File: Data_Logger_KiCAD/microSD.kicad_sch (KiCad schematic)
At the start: 9 parts, among them J3 Micro_SD_Card

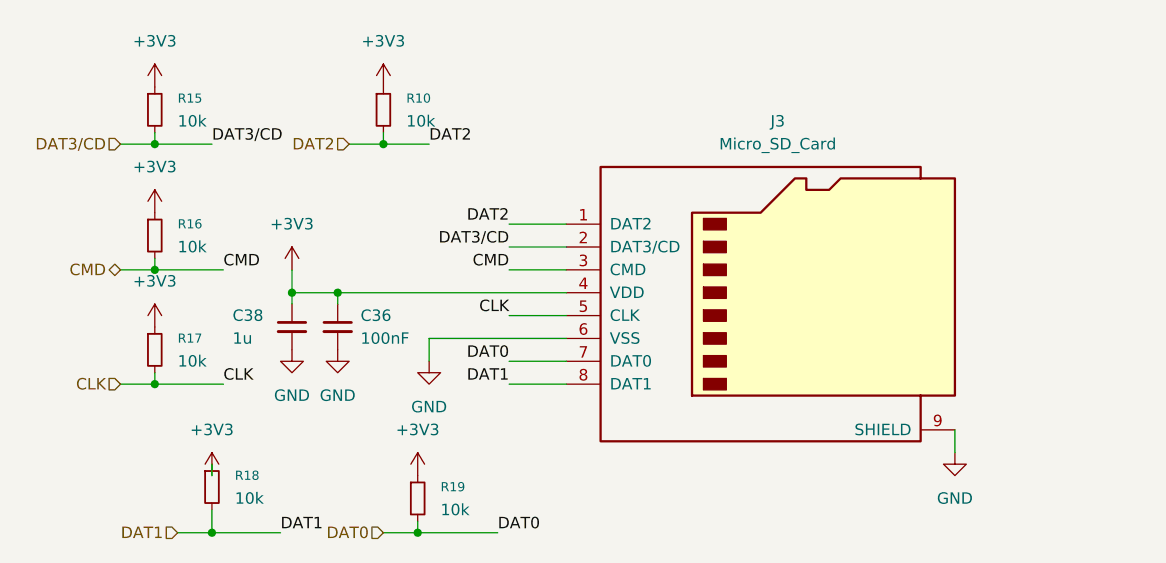
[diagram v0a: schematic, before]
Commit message: footprint + sd tweaks
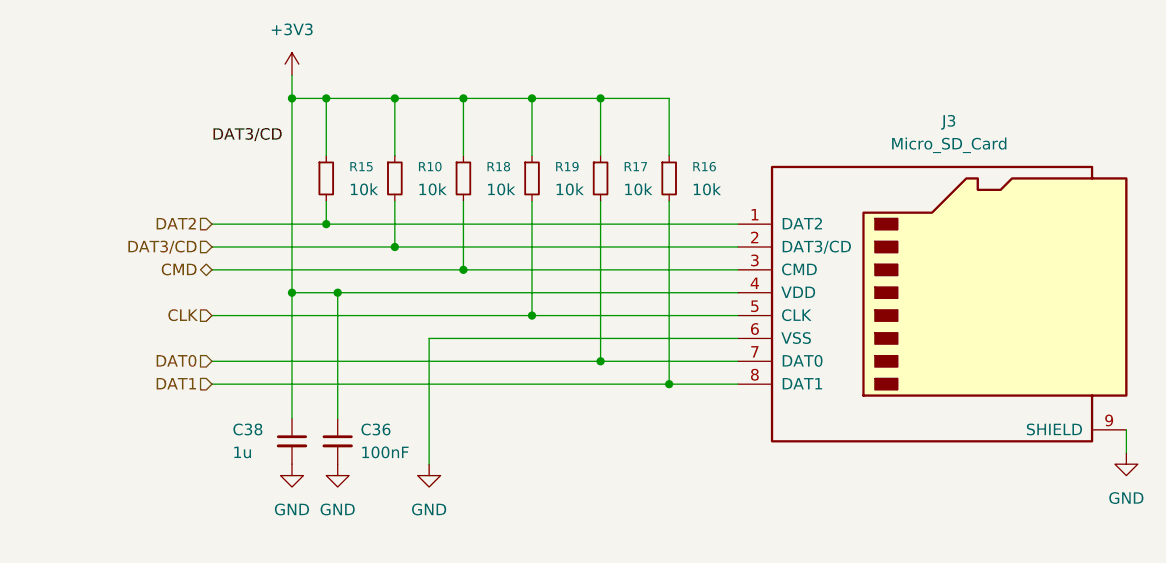
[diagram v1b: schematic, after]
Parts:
- J3: footprint Connector_Card:microSD_HC_Molex_104031-0811 -> Connector_Card:microSD_HC_Molex_47219-2001; digikey https://www.digikey.com/en/products/detail/molex/1040310811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 -> https://www.digikey.com/en/products/detail/molex/0472192001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
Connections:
- net CLK: now also R19.2; no longer R17.2
- net CMD: now also R18.2; no longer R16.2
- net DAT0: now also R17.2; no longer R19.2
- net DAT1: now also R16.2; no longer R18.2
- net DAT2: now also R15.2; no longer R10.2
- net DAT3/CD: now also R10.2; no longer R15.2
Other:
- moved on the sheet: C36, C38, J3, R10, R15, R16, R17, R18, R19

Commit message: more layout
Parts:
- removed R19: 10k, Resistor_SMD:R_0402_1005Metric, symbol Device:R_Small
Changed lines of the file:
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@@
-	)
-	(junction
-		(at 95.25 69.85)
-		(diameter 0)
-		(color 0 0 0 0)
 	)
 	(junction
@@
 	)
 	(junction
-		(at 95.25 45.72)
-		(diameter 0)
-		(color 0 0 0 0)
-	)
-	(junction
 		(at 80.01 45.72)
 		(diameter 0)
@@
 	(wire
 		(pts
-			(xy 87.63 45.72) (xy 95.25 45.72)
+			(xy 87.63 45.72) (xy 102.87 45.72)
 		)
 		(stroke
@@
 	(wire
 		(pts
-			(xy 95.25 45.72) (xy 95.25 52.07)
-		)
-		(stroke
-			(width 0)
-			(type default)
-		)
-	)
-	(wire
-		(pts
-			(xy 95.25 69.85) (xy 118.11 69.85)
-		)
-		(stroke
-			(width 0)
-			(type default)
-		)
-	)
-	(wire
-		(pts
 			(xy 59.69 74.93) (xy 102.87 74.93)
 		)
@@
 	(wire
 		(pts
-			(xy 59.69 69.85) (xy 95.25 69.85)
+			(xy 59.69 69.85) (xy 118.11 69.85)
 		)
 		(stroke
@@
 	(wire
 		(pts
-			(xy 95.25 57.15) (xy 95.25 69.85)
-		)
-		(stroke
-			(width 0)
-			(type default)
-		)
-	)
-	(wire
-		(pts
 			(xy 110.49 57.15) (xy 110.49 77.47)
 		)
@@
 	(wire
 		(pts
-			(xy 95.25 45.72) (xy 102.87 45.72)
-		)
-		(stroke
-			(width 0)
-			(type default)
-		)
-	)
-	(wire
-		(pts
 			(xy 102.87 45.72) (xy 102.87 52.07)
 		)
@@
 			(width 0)
 			(type default)
-		)
-	)
-	(label "DAT3{slash}CD"
-		(at 59.69 50.8 0)
-		(effects
-			(font
-				(size 1.27 1.27)
-			)
-			(justify left bottom)
 		)
 	)
@@
 					(unit 1)
 				)
-			)
-		)
-	)
-	(symbol
-		(lib_id "Device:R_Small")
-		(at 95.25 54.61 0)
-		(unit 1)
-		(exclude_from_sim no)
-		(in_bom yes)
-		(on_board yes)
-		(dnp no)
-		(fields_autoplaced yes)
-		(property "Reference" "R19"
-			(at 97.79 53.3399 0)
-			(effects
-				(font
-					(size 1.016 1.016)
-				)
-				(justify left)
-			)
-		)
-		(property "Value" "10k"
-			(at 97.79 55.8799 0)
-			(effects
-				(font
-					(size 1.27 1.27)
-				)
-				(justify left)
-			)
-		)
-		(property "Footprint" "Resistor_SMD:R_0402_1005Metric"
-			(at 95.25 54.61 0)
-			(effects
-				(font
-					(size 1.27 1.27)
-				)
-				(hide yes)
-			)
-		)
-		(property "Datasheet" "~"
-			(at 95.25 54.61 0)
-			(effects
-				(font
-					(size 1.27 1.27)
-				)
-				(hide yes)
-			)
-		)
-		(property "Description" "Resistor, small symbol"
-			(at 95.25 54.61 0)
-			(effects
-				(font
-					(size 1.27 1.27)
-				)
-				(hide yes)
-			)
-		)
-		(pin "1"
-		)
-		(pin "2"
-		)
-		(instances
-			(project "Data_Logger_Board"
-				(path "/db968e42-3ace-4cc9-9096-9d8f48135c40/795ab2be-9db7-4254-b05c-ac2b60177344/ac1a2286-0136-4664-9bd1-efd641230ecb"
-					(reference "R19")
-					(unit 1)
-				)

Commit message: review LCSC fields
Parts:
- J3: LCSC (none) -> C164170
- R10, R15, R16, R17, R18: LCSC (none) -> C25744
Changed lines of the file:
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@@
+			)
+		)
+		(property "LCSC" "C25744"
+			(at 87.63 54.61 0)
+			(effects
+				(font
+					(size 1.27 1.27)
+				)
+				(hide yes)
 			)
 		)
@@
 			)
 		)
+		(property "LCSC" "C164170"
+			(at 140.97 67.31 0)
+			(effects
+				(font
+					(size 1.27 1.27)
+				)
+				(hide yes)
+			)
+		)
 		(pin "6"
 		)
@@
 			)
 		)
+		(property "LCSC" "C25744"
+			(at 102.87 54.61 0)
+			(effects
+				(font
+					(size 1.27 1.27)
+				)
+				(hide yes)
+			)
+		)
 		(pin "1"
 		)
@@
 			)
 		)
+		(property "LCSC" "C25744"
+			(at 110.49 54.61 0)
+			(effects
+				(font
+					(size 1.27 1.27)
+				)
+				(hide yes)
+			)
+		)
 		(pin "1"
 		)
@@
 			)
 		)
+		(property "LCSC" "C25744"
+			(at 80.01 54.61 0)
+			(effects
+				(font
+					(size 1.27 1.27)
+				)
+				(hide yes)
+			)
+		)
 		(pin "1"
 		)
@@
 			(at 72.39 54.61 0)
 			(effects
+				(font
+					(size 1.27 1.27)
+				)
+				(hide yes)
+			)
+		)
+		(property "LCSC" "C25744"
+			(at 72.39 54.61 0)
+			(effects

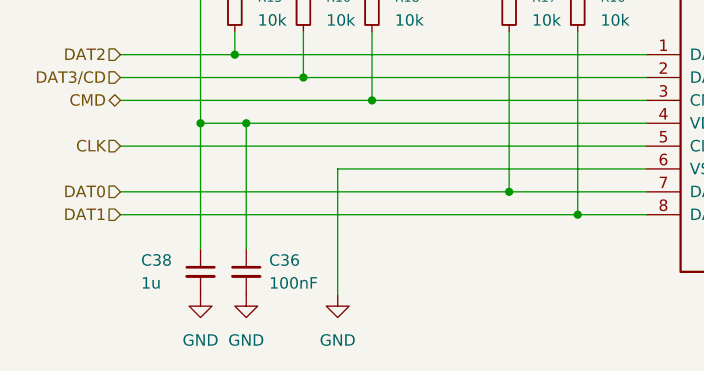
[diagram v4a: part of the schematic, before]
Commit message: remove units for extraction
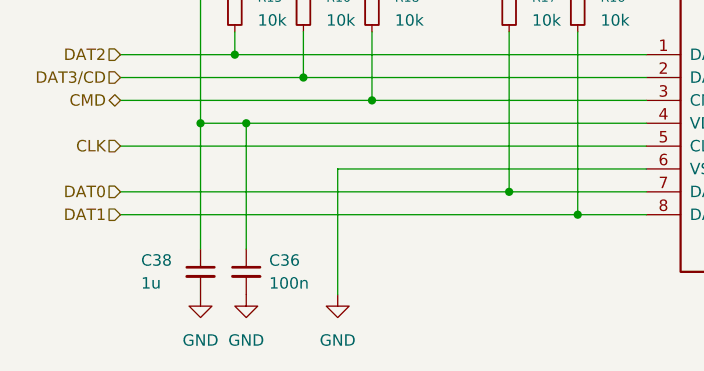
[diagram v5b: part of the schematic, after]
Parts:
- C36: value 100nF -> 100n
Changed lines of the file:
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@@
 			)
 		)
-		(property "Value" "100nF"
+		(property "Value" "100n"
 			(at 76.2 85.0962 0)
 			(effects
